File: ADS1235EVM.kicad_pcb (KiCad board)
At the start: 2 copper layers, 50 x 25 mm, 64 parts, among them J1 Conn_01x04_Pin, J2 Conn_01x11_Pin, U1 ADS1235QWRHMRQ1, U2 LM27762, U5 UCC27524DGN

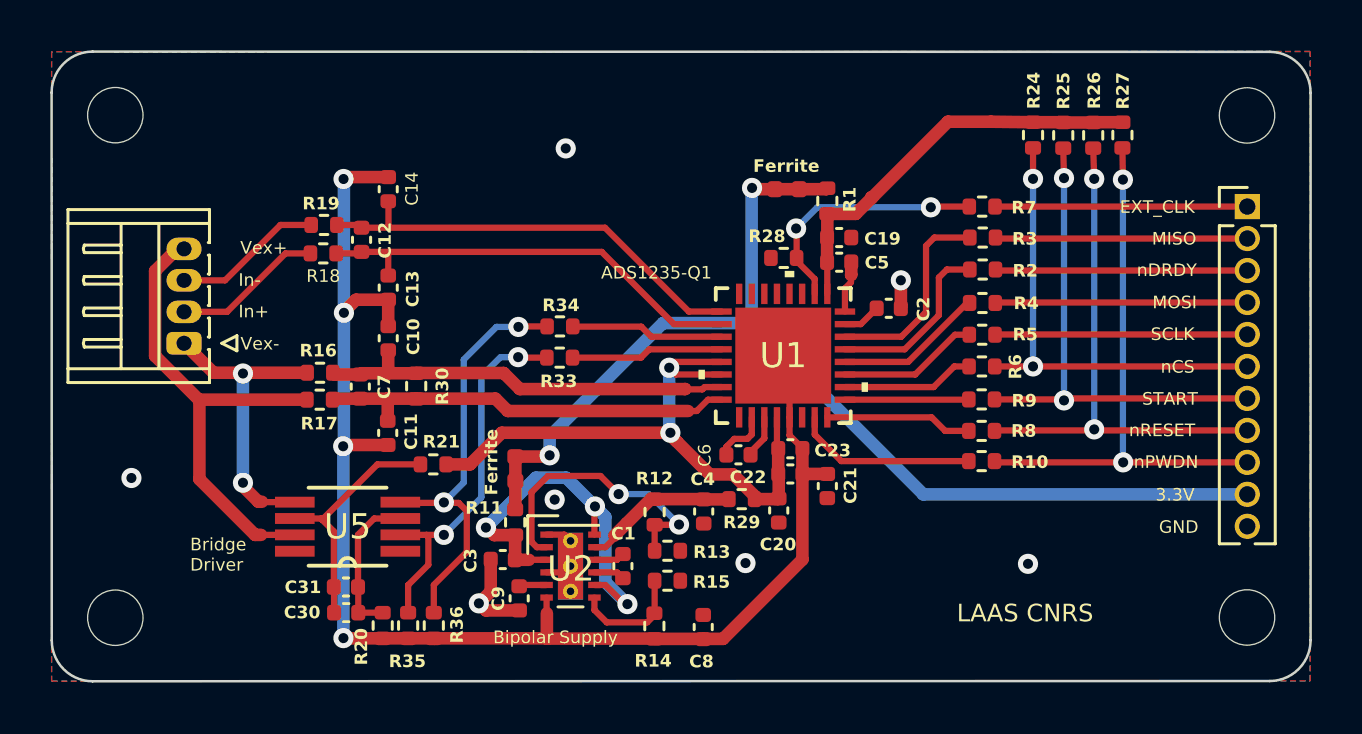
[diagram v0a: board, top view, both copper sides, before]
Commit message: PCB - Add of 2 jumpers to handle AC & DC excitation
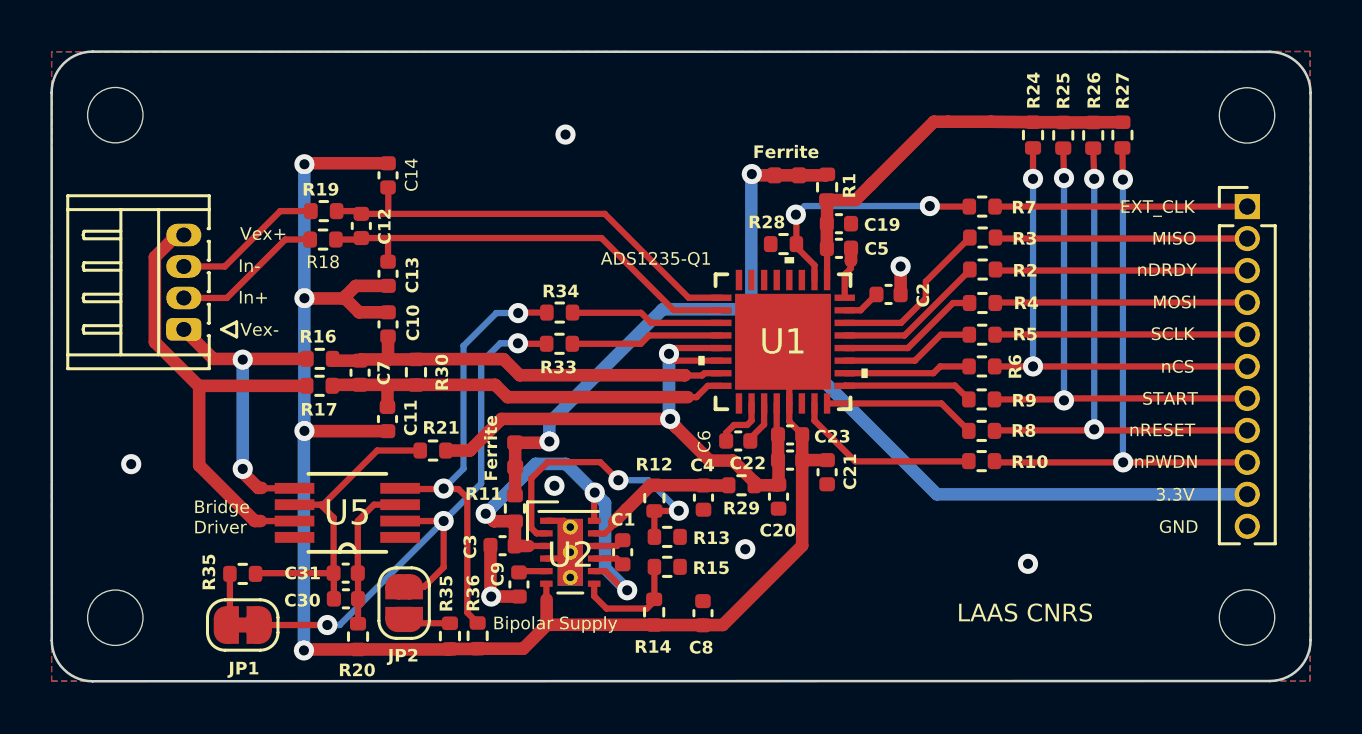
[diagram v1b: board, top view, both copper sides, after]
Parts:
- added JP1: SolderJumper-2_P1.3mm_Bridged_RoundedPad1.0x1.5mm, Jumper:SolderJumper-2_P1.3mm_Bridged_RoundedPad1.0x1.5mm, F.Cu at (107.6, 122.8)
- added JP2: SolderJumper-2_P1.3mm_Open_RoundedPad1.0x1.5mm, Jumper:SolderJumper-2_P1.3mm_Open_RoundedPad1.0x1.5mm, F.Cu at (114.0, 121.9)
- added R35: 100k, Resistor_SMD:R_0402_1005Metric, F.Cu at (107.6, 120.7)
- moved R36 1.79 mm to (116.9, 123.2)
- moved R35 1.71 mm to (115.8, 123.2)
- moved R20 1.07 mm to (112.2, 123.2)
- moved C13 0.55 mm to (113.4, 108.8)
- moved C4 0.55 mm to (125.9, 117.7)
- moved R1 0.55 mm to (130.8, 105.4)
- moved R18 0.55 mm to (110.8, 107.5)
- moved R33 0.55 mm to (120.2, 111.6)
- moved C1 0.55 mm to (122.7, 119.9)
- moved C31 0.55 mm to (111.7, 120.7)
- moved C6 0.55 mm to (127.3, 115.5)
- moved R15 0.55 mm to (124.5, 120.5)
- moved U2 0.55 mm to (120.6, 119.9)
- moved U5 0.55 mm to (111.7, 118.3)
- moved C10 0.55 mm to (113.4, 110.8)
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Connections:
- R35 pad 2: Net-(U5-INA) -> jump2
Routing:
- net Net-(U5-INA): track 15.2 -> 24.6 mm, vias 2 -> 3
- net /-2.5V: track 55.5 -> 63.6 mm
- net Net-(U5-VDD): track 9.83 -> 12.9 mm
- net jump1: track 0.00 -> 2.09 mm
- net jump2: track 0.00 -> 1.88 mm
- net /MISO: track 8.13 -> 6.76 mm
- net /nDRDY: track 7.15 -> 6.07 mm
- net Net-(U5-INB): track 17.3 -> 18.0 mm
- net GND: track 8.93 -> 8.41 mm

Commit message: PCB - Components placement optimisation & add of GND vias
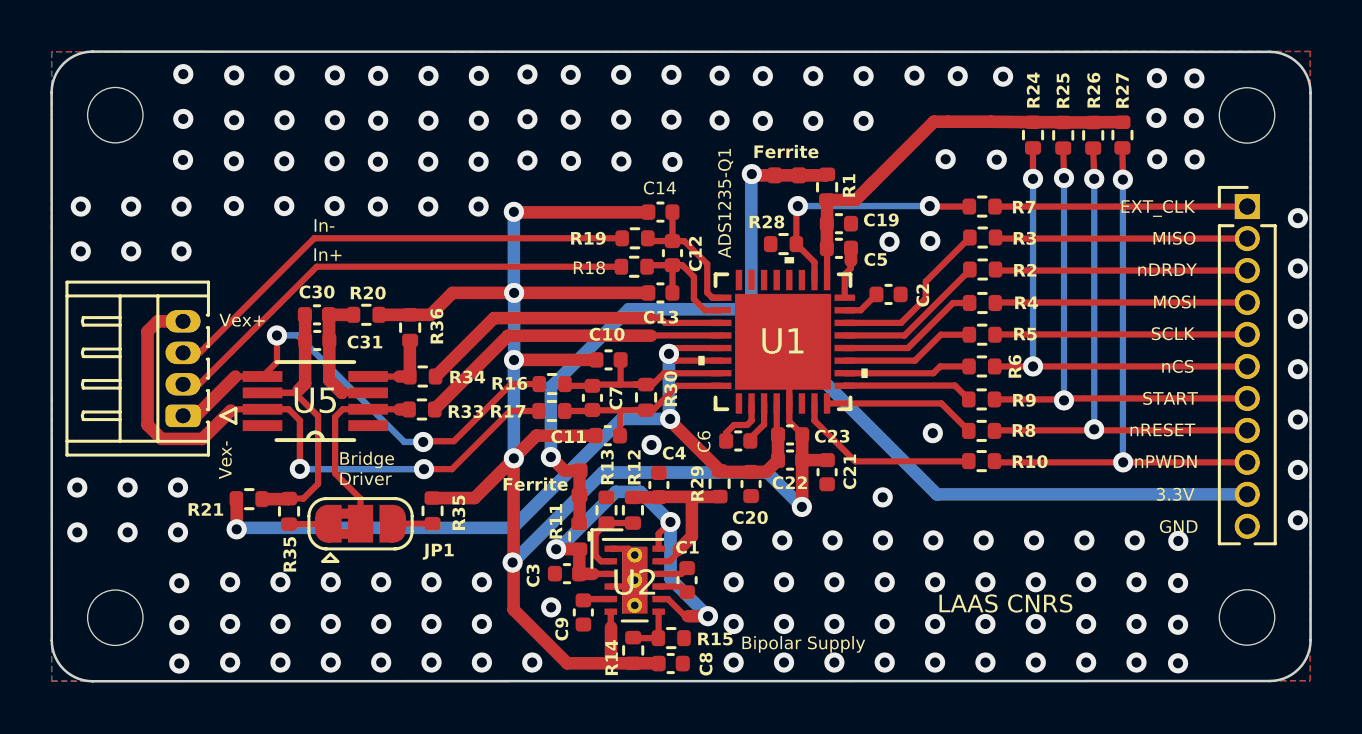
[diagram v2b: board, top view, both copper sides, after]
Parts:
- removed JP2: SolderJumper-2_P1.3mm_Open_RoundedPad1.0x1.5mm, Jumper:SolderJumper-2_P1.3mm_Open_RoundedPad1.0x1.5mm
- JP1: value SolderJumper-2_P1.3mm_Bridged_RoundedPad1.0x1.5mm -> SolderJumper-3_P1.3mm_Bridged2Bar12_RoundedPad1.0x1.5mm; footprint Jumper:SolderJumper-2_P1.3mm_Bridged_RoundedPad1.0x1.5mm -> Jumper:SolderJumper-3_P1.3mm_Bridged2Bar12_RoundedPad1.0x1.5mm
- moved R20 12.8 mm to (112.5, 110.5), turned to 0 degrees
- moved R36 12.5 mm to (114.2, 111.0), turned to -90 degrees
- moved R18 12.4 mm to (123.1, 108.5)
- moved R19 12.4 mm to (123.2, 107.4)
- moved C12 12.4 mm to (124.7, 108.0)
- moved C30 11.3 mm to (110.5, 110.5)
- moved C14 10.9 mm to (124.2, 106.4), turned to 180 degrees
- moved C13 10.8 mm to (124.2, 109.6), turned to 0 degrees
- moved C31 9.31 mm to (110.5, 111.5)
- moved C7 9.28 mm to (121.5, 113.8)
- moved R17 9.28 mm to (119.9, 114.3)
- moved R16 9.28 mm to (119.9, 113.2)
- moved R30 9.19 mm to (123.6, 113.7)
- moved C10 8.87 mm to (122.1, 112.2), turned to 0 degrees
- moved C11 8.77 mm to (122.1, 115.2), turned to 180 degrees
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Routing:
- net Net-(U5-INA): track 24.6 -> 7.73 mm, vias 3 -> 0
- net Net-(U5-INB): track 18.0 -> 2.98 mm, vias 2 -> 0
- net Net-(J1-Pin_2): track 5.98 -> 19.5 mm
- net Net-(J1-Pin_3): track 5.96 -> 19.3 mm
- net Net-(U1-AIN4): track 17.6 -> 5.34 mm
- net Net-(U1-AIN5): track 17.8 -> 5.71 mm
- net /Avdd: track 25.6 -> 35.1 mm, vias 2 -> 3
- net /-2.5V: track 63.6 -> 73.0 mm, vias 4 -> 6
- net Net-(U1-REFN0): track 16.9 -> 7.89 mm
- net Net-(U1-REFP0): track 16.8 -> 8.13 mm
- net Net-(U2-FB+): track 11.8 -> 3.23 mm, vias 2 -> 0
- net Net-(J1-Pin_1): track 12.3 -> 19.1 mm
- net /ACX1: track 6.07 -> 12.6 mm
- net /ACX2: track 6.08 -> 12.4 mm
- net Net-(J1-Pin_4): track 19.5 -> 24.8 mm, vias 0 -> 2
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
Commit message: Association Schematic & PCB
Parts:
- JP1: value SolderJumper-3_P1.3mm_Bridged2Bar12_RoundedPad1.0x1.5mm -> Jumper_3_Bridged12; footprint Jumper:SolderJumper-3_P1.3mm_Bridged2Bar12_RoundedPad1.0x1.5mm -> Jumper:SolderJumper-3_P1.3mm_Bridged12_RoundedPad1.0x1.5mm
- moved C14 3.21 mm to (124.2, 109.6)
- moved C13 3.18 mm to (124.2, 106.4)
- moved R19 1.12 mm to (123.2, 108.5)
- moved R18 1.10 mm to (123.2, 107.4)
- moved C11 0.66 mm to (122.5, 114.8), turned to -90 degrees
- turned C12 to -90 degrees
- turned R22 to 90 degrees
- renumbered R35 to R22
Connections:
- net jump2 renamed Net-(JP1-B)
- C12 pad 1: Net-(U1-AIN4) -> Net-(U1-AIN5)
- C12 pad 2: Net-(U1-AIN5) -> Net-(U1-AIN4)
- C13 pad 2: Net-(U1-AIN4) -> Net-(U1-AIN5)
- C14 pad 1: Net-(U1-AIN5) -> Net-(U1-AIN4)
- JP1 pad 1: jump1 -> Net-(JP1-A)
- R18 pad 1: Net-(J1-Pin_2) -> Net-(J1-Pin_3)
- R18 pad 2: Net-(U1-AIN4) -> Net-(U1-AIN5)
- R19 pad 1: Net-(J1-Pin_3) -> Net-(J1-Pin_2)
- R19 pad 2: Net-(U1-AIN5) -> Net-(U1-AIN4)
- R22 pad 1: Net-(U5-VDD) -> Net-(JP1-A)
- R22 pad 2: jump1 -> Net-(U5-VDD)
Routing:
- net jump1: track 1.55 -> 0.00 mm
- net Net-(JP1-A): track 0.00 -> 1.55 mm
- net Net-(U1-REFP0): track 8.13 -> 7.11 mm
- net /3V3a: track 17.0 -> 16.0 mm
- net /-2.5V: track 73.0 -> 72.5 mm
- net /Avdd: track 35.1 -> 35.7 mm, vias 3 -> 4

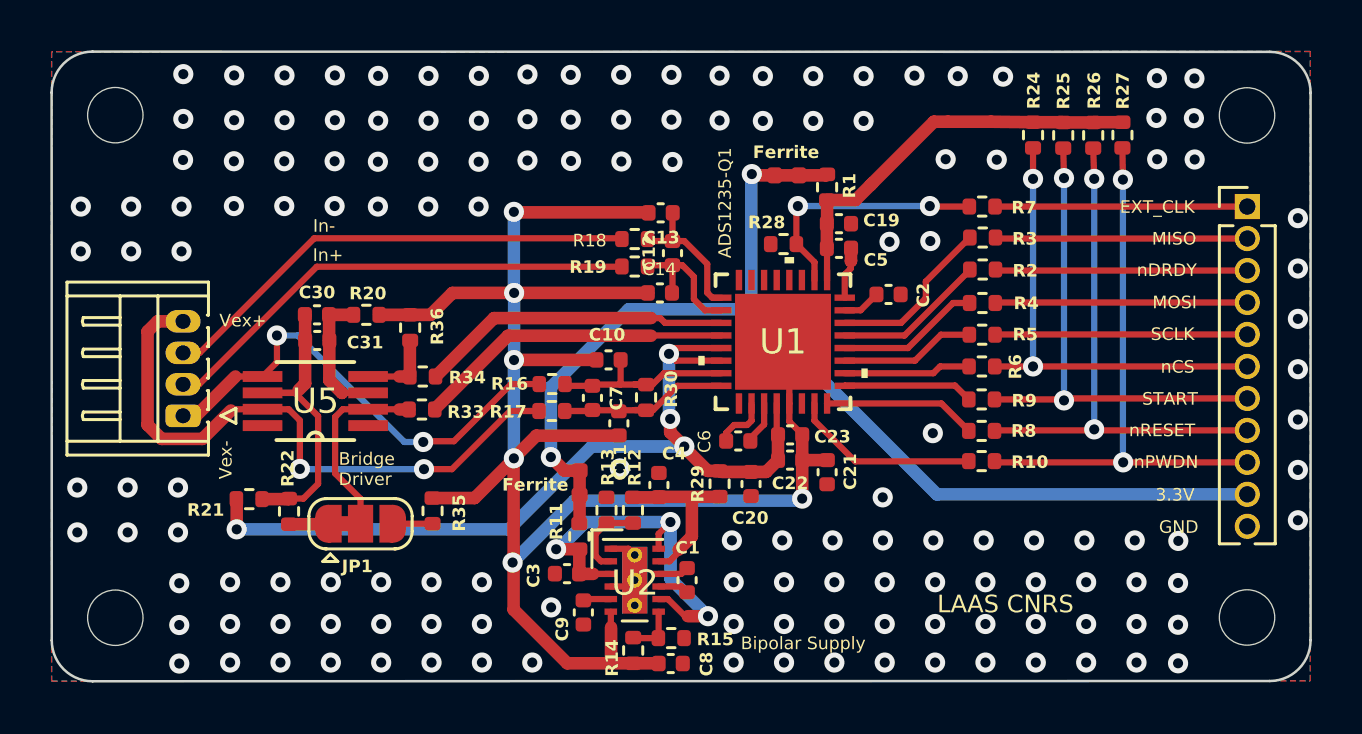
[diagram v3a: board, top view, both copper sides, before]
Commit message: Add of 2.54mm SPI connector & open jumper
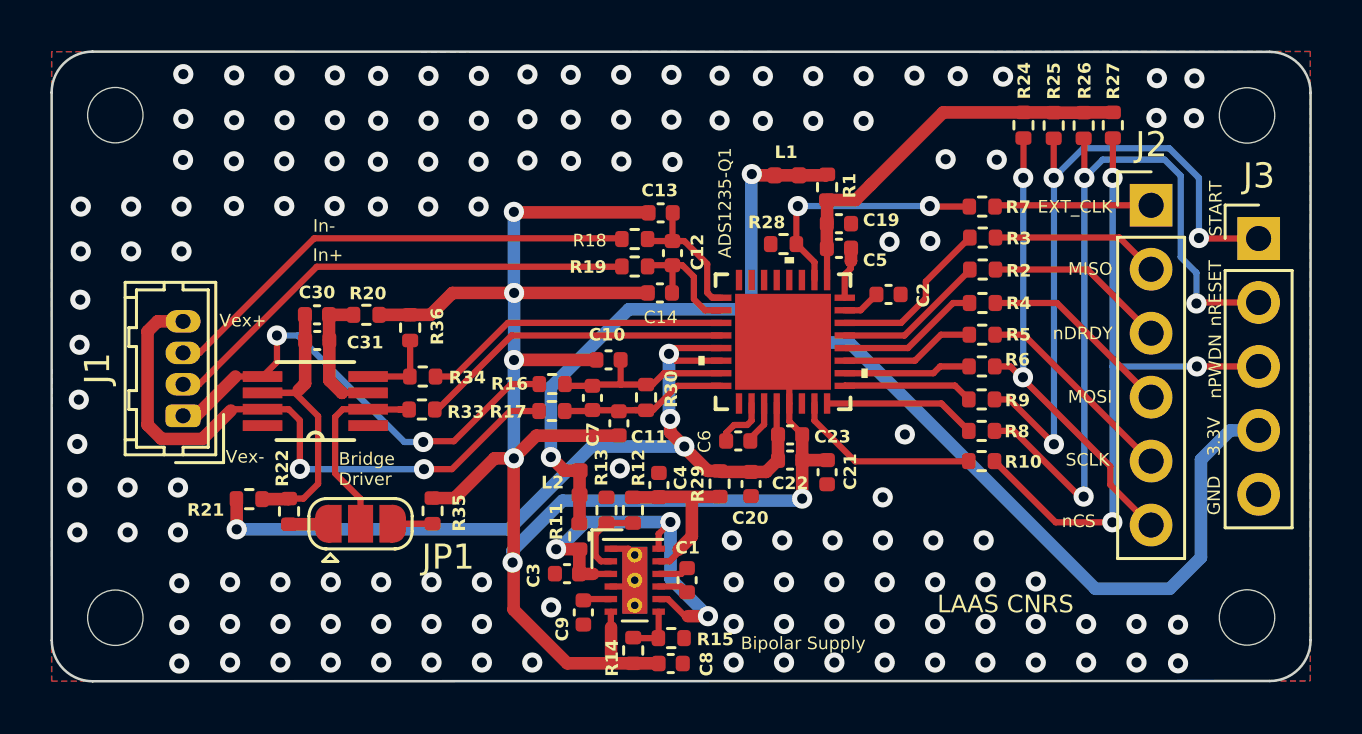
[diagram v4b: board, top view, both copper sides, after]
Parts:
- added J3: Conn_01x05_Pin, Connector_PinHeader_2.54mm:PinHeader_1x05_P2.54mm_Vertical, F.Cu at (147.9, 107.4)
- J1: footprint Connector_Hirose:Hirose_DF13-04P-1.25DS_1x04_P1.25mm_Horizontal -> Connector_Hirose:Hirose_DF13-04P-1.25DSA_1x04_P1.25mm_Vertical
- J2: value Conn_01x11_Pin -> Conn_01x06_Pin; footprint Connector_PinHeader_1.27mm:PinHeader_1x11_P1.27mm_Vertical -> Connector_PinHeader_2.54mm:PinHeader_1x06_P2.54mm_Vertical
- JP1: footprint Jumper:SolderJumper-3_P1.3mm_Bridged12_RoundedPad1.0x1.5mm -> Jumper:SolderJumper-3_P1.3mm_Open_RoundedPad1.0x1.5mm
- L1, L2: renamed from Ferrite; value L_0402_1005Metric -> 0
- moved J2 3.82 mm to (143.7, 106.1)
- moved R24 0.54 mm to (138.6, 102.9)
- moved R27 0.54 mm to (142.2, 102.9)
- moved R25 0.54 mm to (139.8, 102.9)
- moved R26 0.54 mm to (141.0, 102.9)
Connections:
- R10 pad 2: Net-(J2-Pin_9) -> Net-(J3-Pin_3)
- R25 pad 2: Net-(J2-Pin_7) -> Net-(J3-Pin_1)
- R26 pad 2: Net-(J2-Pin_8) -> Net-(J3-Pin_2)
- R27 pad 2: Net-(J2-Pin_9) -> Net-(J3-Pin_3)
- R8 pad 2: Net-(J2-Pin_8) -> Net-(J3-Pin_2)
- R9 pad 2: Net-(J2-Pin_7) -> Net-(J3-Pin_1)
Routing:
- net Net-(J3-Pin_2): track 0.00 -> 31.1 mm, vias 0 -> 3
- net Net-(J3-Pin_3): track 0.00 -> 27.1 mm, vias 0 -> 3
- net Net-(J3-Pin_1): track 0.00 -> 27.0 mm, vias 0 -> 3
- net Net-(J2-Pin_9): track 22.7 -> 0.00 mm, vias 2 -> 0
- net Net-(J2-Pin_8): track 21.4 -> 0.00 mm, vias 2 -> 0
- net Net-(J2-Pin_7): track 20.2 -> 0.00 mm, vias 2 -> 0
- net /3V3: track 48.7 -> 55.4 mm
- net Net-(J2-Pin_1): track 10.0 -> 6.22 mm
- net Net-(J2-Pin_2): track 10.0 -> 6.70 mm
- net Net-(J2-Pin_3): track 10.0 -> 7.23 mm
- net Net-(J2-Pin_4): track 10.0 -> 7.77 mm
- net Net-(J2-Pin_5): track 10.0 -> 8.29 mm
- net GND: track 4.17 -> 4.24 mm, vias 145 -> 133

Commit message: KiCAD - Change ferrite net names
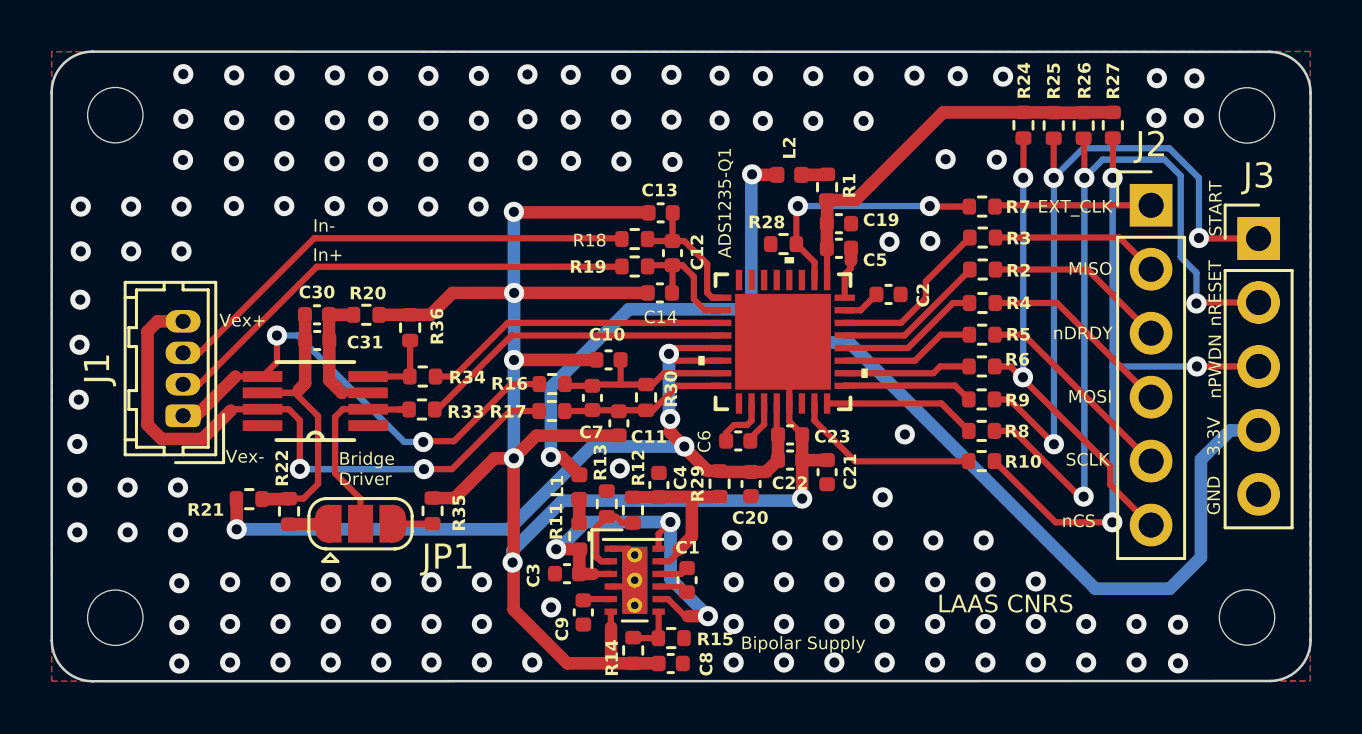
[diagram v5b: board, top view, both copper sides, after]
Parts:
- moved L1 14.9 mm to (121.0, 117.3), turned to -90 degrees
- moved L2 14.8 mm to (129.3, 104.9), turned to 0 degrees
- moved R13 0.25 mm to (122.0, 118.0)
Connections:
- L1 pad 2: /3V3 -> /3V3L1
- L2 pad 2: /3V3 -> /3V3L2
- R1 pad 2: /3V3 -> /3V3L2
- R11 pad 1: /3V3 -> /3V3L1
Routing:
- net /3V3: track 55.4 -> 51.3 mm
- net /3V3L2: track 0.00 -> 1.02 mm
- net /3V3L1: track 0.00 -> 0.98 mm
